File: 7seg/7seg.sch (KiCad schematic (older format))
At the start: 9 parts, among them J1 9pin_header, U1 LTS-4031JR, U2 LTS-4031JR, U3 LTS-4031JR, U4 LTS-4031JR, U5 LTS-4031JR, U6 LTS-4031JR, U7 LTS-4031JR, U8 LTS-4031JR

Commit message: 7-segment layout
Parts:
- added H1, H2, H3, H4: MountingHole, MountingHole:MountingHole_2.2mm_M2_Pad, symbol Mechanical:MountingHole
- U1, U2, U3, U4, U5, U6, U7, U8: footprint (none) -> SamacSys_Parts:DIPS762W50P254L1290H725Q10N
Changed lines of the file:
@@
 F 0 "U1" H 1550 2565 50  0000 C CNN
 F 1 "LTS-4031JR" H 1550 2474 50  0000 C CNN
-F 2 "" H 1550 2450 50  0001 C CNN
+F 2 "SamacSys_Parts:DIPS762W50P254L1290H725Q10N" H 1550 2450 50  0001 C CNN
 F 3 "" H 1550 2450 50  0001 C CNN
 	1    1550 2450
@@
 F 0 "U2" H 2750 2565 50  0000 C CNN
 F 1 "LTS-4031JR" H 2750 2474 50  0000 C CNN
-F 2 "" H 2750 2450 50  0001 C CNN
+F 2 "SamacSys_Parts:DIPS762W50P254L1290H725Q10N" H 2750 2450 50  0001 C CNN
 F 3 "" H 2750 2450 50  0001 C CNN
 	1    2750 2450
@@
 F 0 "U3" H 3950 2565 50  0000 C CNN
 F 1 "LTS-4031JR" H 3950 2474 50  0000 C CNN
-F 2 "" H 3950 2450 50  0001 C CNN
+F 2 "SamacSys_Parts:DIPS762W50P254L1290H725Q10N" H 3950 2450 50  0001 C CNN
 F 3 "" H 3950 2450 50  0001 C CNN
 	1    3950 2450
@@
 F 0 "U4" H 5150 2565 50  0000 C CNN
 F 1 "LTS-4031JR" H 5150 2474 50  0000 C CNN
-F 2 "" H 5150 2450 50  0001 C CNN
+F 2 "SamacSys_Parts:DIPS762W50P254L1290H725Q10N" H 5150 2450 50  0001 C CNN
 F 3 "" H 5150 2450 50  0001 C CNN
 	1    5150 2450
@@
 F 0 "U5" H 6300 2565 50  0000 C CNN
 F 1 "LTS-4031JR" H 6300 2474 50  0000 C CNN
-F 2 "" H 6300 2450 50  0001 C CNN
+F 2 "SamacSys_Parts:DIPS762W50P254L1290H725Q10N" H 6300 2450 50  0001 C CNN
 F 3 "" H 6300 2450 50  0001 C CNN
 	1    6300 2450
@@
 F 0 "U6" H 7450 2565 50  0000 C CNN
 F 1 "LTS-4031JR" H 7450 2474 50  0000 C CNN
-F 2 "" H 7450 2450 50  0001 C CNN
+F 2 "SamacSys_Parts:DIPS762W50P254L1290H725Q10N" H 7450 2450 50  0001 C CNN
 F 3 "" H 7450 2450 50  0001 C CNN
 	1    7450 2450
@@
 F 0 "U7" H 8600 2565 50  0000 C CNN
 F 1 "LTS-4031JR" H 8600 2474 50  0000 C CNN
-F 2 "" H 8600 2450 50  0001 C CNN
+F 2 "SamacSys_Parts:DIPS762W50P254L1290H725Q10N" H 8600 2450 50  0001 C CNN
 F 3 "" H 8600 2450 50  0001 C CNN
 	1    8600 2450
@@
 F 0 "U8" H 9750 2565 50  0000 C CNN
 F 1 "LTS-4031JR" H 9750 2474 50  0000 C CNN
-F 2 "" H 9750 2450 50  0001 C CNN
+F 2 "SamacSys_Parts:DIPS762W50P254L1290H725Q10N" H 9750 2450 50  0001 C CNN
 F 3 "" H 9750 2450 50  0001 C CNN
 	1    9750 2450
@@
 Wire Wire Line
 	6700 1700 7850 1700
+$Comp
+L Mechanical:MountingHole H1
+U 1 1 61664F25
+P 3000 750
+F 0 "H1" H 3100 796 50  0000 L CNN
+F 1 "MountingHole" H 3100 705 50  0000 L CNN
+F 2 "MountingHole:MountingHole_2.2mm_M2_Pad" H 3000 750 50  0001 C CNN
+F 3 "~" H 3000 750 50  0001 C CNN
+	1    3000 750
+	1    0    0    -1
+$EndComp
+$Comp
+L Mechanical:MountingHole H2
+U 1 1 61679F30
+P 3000 950
+F 0 "H2" H 3100 996 50  0000 L CNN
+F 1 "MountingHole" H 3100 905 50  0000 L CNN
+F 2 "MountingHole:MountingHole_2.2mm_M2_Pad" H 3000 950 50  0001 C CNN
+F 3 "~" H 3000 950 50  0001 C CNN
+	1    3000 950
+	1    0    0    -1
+$EndComp
+$Comp
+L Mechanical:MountingHole H3
+U 1 1 6167A224
+P 3000 1150
+F 0 "H3" H 3100 1196 50  0000 L CNN
+F 1 "MountingHole" H 3100 1105 50  0000 L CNN
+F 2 "MountingHole:MountingHole_2.2mm_M2_Pad" H 3000 1150 50  0001 C CNN
+F 3 "~" H 3000 1150 50  0001 C CNN
+	1    3000 1150
+	1    0    0    -1
+$EndComp
+$Comp
+L Mechanical:MountingHole H4
+U 1 1 6167A7D7
+P 3000 1350
+F 0 "H4" H 3100 1396 50  0000 L CNN
+F 1 "MountingHole" H 3100 1305 50  0000 L CNN
+F 2 "MountingHole:MountingHole_2.2mm_M2_Pad" H 3000 1350 50  0001 C CNN
+F 3 "~" H 3000 1350 50  0001 C CNN
+	1    3000 1350
+	1    0    0    -1
+$EndComp
 $EndSCHEMATC

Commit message: more library changes
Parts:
- H1, H2, H3, H4: footprint MountingHole:MountingHole_2.2mm_M2_Pad -> footprints:MountingHole_2.2mm_M2_Pad
- J1: footprint HDRV9W63P0X254_1X9_2286X369X950P -> footprints:header
- U1, U2, U3, U4, U5, U6, U7, U8: footprint SamacSys_Parts:DIPS762W50P254L1290H725Q10N -> footprints:7seg
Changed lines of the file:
@@
 F 0 "U1" H 1550 2565 50  0000 C CNN
 F 1 "LTS-4031JR" H 1550 2474 50  0000 C CNN
-F 2 "SamacSys_Parts:DIPS762W50P254L1290H725Q10N" H 1550 2450 50  0001 C CNN
+F 2 "footprints:7seg" H 1550 2450 50  0001 C CNN
 F 3 "" H 1550 2450 50  0001 C CNN
 	1    1550 2450
-	1    0    0    -1
-$EndComp
-$Comp
-L 477_7seg_symbols:LTS-4031JR U2
-U 1 1 615ED9B1
-P 2750 2450
-F 0 "U2" H 2750 2565 50  0000 C CNN
-F 1 "LTS-4031JR" H 2750 2474 50  0000 C CNN
-F 2 "SamacSys_Parts:DIPS762W50P254L1290H725Q10N" H 2750 2450 50  0001 C CNN
-F 3 "" H 2750 2450 50  0001 C CNN
-	1    2750 2450
-	1    0    0    -1
-$EndComp
-$Comp
-L 477_7seg_symbols:LTS-4031JR U3
-U 1 1 615EE8CF
-P 3950 2450
-F 0 "U3" H 3950 2565 50  0000 C CNN
-F 1 "LTS-4031JR" H 3950 2474 50  0000 C CNN
-F 2 "SamacSys_Parts:DIPS762W50P254L1290H725Q10N" H 3950 2450 50  0001 C CNN
-F 3 "" H 3950 2450 50  0001 C CNN
-	1    3950 2450
-	1    0    0    -1
-$EndComp
-$Comp
-L 477_7seg_symbols:LTS-4031JR U4
-U 1 1 615EF228
-P 5150 2450
-F 0 "U4" H 5150 2565 50  0000 C CNN
-F 1 "LTS-4031JR" H 5150 2474 50  0000 C CNN
-F 2 "SamacSys_Parts:DIPS762W50P254L1290H725Q10N" H 5150 2450 50  0001 C CNN
-F 3 "" H 5150 2450 50  0001 C CNN
-	1    5150 2450
-	1    0    0    -1
-$EndComp
-$Comp
-L 477_7seg_symbols:LTS-4031JR U5
-U 1 1 615F0325
-P 6300 2450
-F 0 "U5" H 6300 2565 50  0000 C CNN
-F 1 "LTS-4031JR" H 6300 2474 50  0000 C CNN
-F 2 "SamacSys_Parts:DIPS762W50P254L1290H725Q10N" H 6300 2450 50  0001 C CNN
-F 3 "" H 6300 2450 50  0001 C CNN
-	1    6300 2450
-	1    0    0    -1
-$EndComp
-$Comp
-L 477_7seg_symbols:LTS-4031JR U6
-U 1 1 615F0C91
-P 7450 2450
-F 0 "U6" H 7450 2565 50  0000 C CNN
-F 1 "LTS-4031JR" H 7450 2474 50  0000 C CNN
-F 2 "SamacSys_Parts:DIPS762W50P254L1290H725Q10N" H 7450 2450 50  0001 C CNN
-F 3 "" H 7450 2450 50  0001 C CNN
-	1    7450 2450
-	1    0    0    -1
-$EndComp
-$Comp
-L 477_7seg_symbols:LTS-4031JR U7
-U 1 1 615F27E9
-P 8600 2450
-F 0 "U7" H 8600 2565 50  0000 C CNN
-F 1 "LTS-4031JR" H 8600 2474 50  0000 C CNN
-F 2 "SamacSys_Parts:DIPS762W50P254L1290H725Q10N" H 8600 2450 50  0001 C CNN
-F 3 "" H 8600 2450 50  0001 C CNN
-	1    8600 2450
-	1    0    0    -1
-$EndComp
-$Comp
-L 477_7seg_symbols:LTS-4031JR U8
-U 1 1 615F702E
-P 9750 2450
-F 0 "U8" H 9750 2565 50  0000 C CNN
-F 1 "LTS-4031JR" H 9750 2474 50  0000 C CNN
-F 2 "SamacSys_Parts:DIPS762W50P254L1290H725Q10N" H 9750 2450 50  0001 C CNN
-F 3 "" H 9750 2450 50  0001 C CNN
-	1    9750 2450
 	1    0    0    -1
 $EndComp
@@
 F 0 "J1" V 5488 672 50  0000 R CNN
 F 1 "9pin_header" V 5397 672 50  0000 R CNN
-F 2 "HDRV9W63P0X254_1X9_2286X369X950P" H 5800 1700 50  0001 L CNN
+F 2 "footprints:header" H 5800 1700 50  0001 L CNN
 F 3 "https://componentsearchengine.com/Datasheets/1/825433-9.pdf" H 5800 1600 50  0001 L CNN
 F 4 "MOD 2 PINHDR 1X9 P." H 5800 1500 50  0001 L CNN "Description"
@@
 	6700 1700 7850 1700
 $Comp
-L Mechanical:MountingHole H1
-U 1 1 61664F25
-P 3000 750
-F 0 "H1" H 3100 796 50  0000 L CNN
-F 1 "MountingHole" H 3100 705 50  0000 L CNN
-F 2 "MountingHole:MountingHole_2.2mm_M2_Pad" H 3000 750 50  0001 C CNN
-F 3 "~" H 3000 750 50  0001 C CNN
-	1    3000 750
-	1    0    0    -1
-$EndComp
-$Comp
-L Mechanical:MountingHole H2
-U 1 1 61679F30
-P 3000 950
-F 0 "H2" H 3100 996 50  0000 L CNN
-F 1 "MountingHole" H 3100 905 50  0000 L CNN
-F 2 "MountingHole:MountingHole_2.2mm_M2_Pad" H 3000 950 50  0001 C CNN
-F 3 "~" H 3000 950 50  0001 C CNN
-	1    3000 950
-	1    0    0    -1
-$EndComp
-$Comp
-L Mechanical:MountingHole H3
-U 1 1 6167A224
-P 3000 1150
-F 0 "H3" H 3100 1196 50  0000 L CNN
-F 1 "MountingHole" H 3100 1105 50  0000 L CNN
-F 2 "MountingHole:MountingHole_2.2mm_M2_Pad" H 3000 1150 50  0001 C CNN
-F 3 "~" H 3000 1150 50  0001 C CNN
-	1    3000 1150
-	1    0    0    -1
-$EndComp
-$Comp
 L Mechanical:MountingHole H4
 U 1 1 6167A7D7
@@
 F 0 "H4" H 3100 1396 50  0000 L CNN
 F 1 "MountingHole" H 3100 1305 50  0000 L CNN
-F 2 "MountingHole:MountingHole_2.2mm_M2_Pad" H 3000 1350 50  0001 C CNN
+F 2 "footprints:MountingHole_2.2mm_M2_Pad" H 3000 1350 50  0001 C CNN
 F 3 "~" H 3000 1350 50  0001 C CNN
 	1    3000 1350
 	1    0    0    -1
 $EndComp
+$Comp
+L 477_7seg_symbols:LTS-4031JR U2
+U 1 1 61670141
+P 2750 2450
+F 0 "U2" H 2750 2565 50  0000 C CNN
+F 1 "LTS-4031JR" H 2750 2474 50  0000 C CNN
+F 2 "footprints:7seg" H 2750 2450 50  0001 C CNN
+F 3 "" H 2750 2450 50  0001 C CNN
+	1    2750 2450
+	1    0    0    -1
+$EndComp
+$Comp
+L 477_7seg_symbols:LTS-4031JR U3
+U 1 1 61670C1A
+P 3950 2450
+F 0 "U3" H 3950 2565 50  0000 C CNN
+F 1 "LTS-4031JR" H 3950 2474 50  0000 C CNN
+F 2 "footprints:7seg" H 3950 2450 50  0001 C CNN
+F 3 "" H 3950 2450 50  0001 C CNN
+	1    3950 2450
+	1    0    0    -1
+$EndComp
+$Comp
+L 477_7seg_symbols:LTS-4031JR U4
+U 1 1 616713BD
+P 5150 2450
+F 0 "U4" H 5150 2565 50  0000 C CNN
+F 1 "LTS-4031JR" H 5150 2474 50  0000 C CNN
+F 2 "footprints:7seg" H 5150 2450 50  0001 C CNN
+F 3 "" H 5150 2450 50  0001 C CNN
+	1    5150 2450
+	1    0    0    -1
+$EndComp
+$Comp
+L 477_7seg_symbols:LTS-4031JR U5
+U 1 1 616717C6
+P 6300 2450
+F 0 "U5" H 6300 2565 50  0000 C CNN
+F 1 "LTS-4031JR" H 6300 2474 50  0000 C CNN
+F 2 "footprints:7seg" H 6300 2450 50  0001 C CNN
+F 3 "" H 6300 2450 50  0001 C CNN
+	1    6300 2450
+	1    0    0    -1
+$EndComp
+$Comp
+L 477_7seg_symbols:LTS-4031JR U6
+U 1 1 61671D60
+P 7450 2450
+F 0 "U6" H 7450 2565 50  0000 C CNN
+F 1 "LTS-4031JR" H 7450 2474 50  0000 C CNN
+F 2 "footprints:7seg" H 7450 2450 50  0001 C CNN
+F 3 "" H 7450 2450 50  0001 C CNN
+	1    7450 2450
+	1    0    0    -1
+$EndComp
+$Comp
+L 477_7seg_symbols:LTS-4031JR U7
+U 1 1 616722D6
+P 8600 2450
+F 0 "U7" H 8600 2565 50  0000 C CNN
+F 1 "LTS-4031JR" H 8600 2474 50  0000 C CNN
+F 2 "footprints:7seg" H 8600 2450 50  0001 C CNN
+F 3 "" H 8600 2450 50  0001 C CNN
+	1    8600 2450
+	1    0    0    -1
+$EndComp
+$Comp
+L 477_7seg_symbols:LTS-4031JR U8
+U 1 1 6167297B
+P 9750 2450
+F 0 "U8" H 9750 2565 50  0000 C CNN
+F 1 "LTS-4031JR" H 9750 2474 50  0000 C CNN
+F 2 "footprints:7seg" H 9750 2450 50  0001 C CNN
+F 3 "" H 9750 2450 50  0001 C CNN
+	1    9750 2450
+	1    0    0    -1
+$EndComp
+$Comp
+L Mechanical:MountingHole H3
+U 1 1 616872D0
+P 3000 1150
+F 0 "H3" H 3100 1196 50  0000 L CNN
+F 1 "MountingHole" H 3100 1105 50  0000 L CNN
+F 2 "footprints:MountingHole_2.2mm_M2_Pad" H 3000 1150 50  0001 C CNN
+F 3 "~" H 3000 1150 50  0001 C CNN
+	1    3000 1150
+	1    0    0    -1
+$EndComp
+$Comp
+L Mechanical:MountingHole H2
+U 1 1 616873EF
+P 3000 950
+F 0 "H2" H 3100 996 50  0000 L CNN
+F 1 "MountingHole" H 3100 905 50  0000 L CNN
+F 2 "footprints:MountingHole_2.2mm_M2_Pad" H 3000 950 50  0001 C CNN
+F 3 "~" H 3000 950 50  0001 C CNN
+	1    3000 950
+	1    0    0    -1
+$EndComp
+$Comp
+L Mechanical:MountingHole H1
+U 1 1 61687670
+P 3000 750
+F 0 "H1" H 3100 796 50  0000 L CNN
+F 1 "MountingHole" H 3100 705 50  0000 L CNN
+F 2 "footprints:MountingHole_2.2mm_M2_Pad" H 3000 750 50  0001 C CNN
+F 3 "~" H 3000 750 50  0001 C CNN
+	1    3000 750
+	1    0    0    -1
+$EndComp

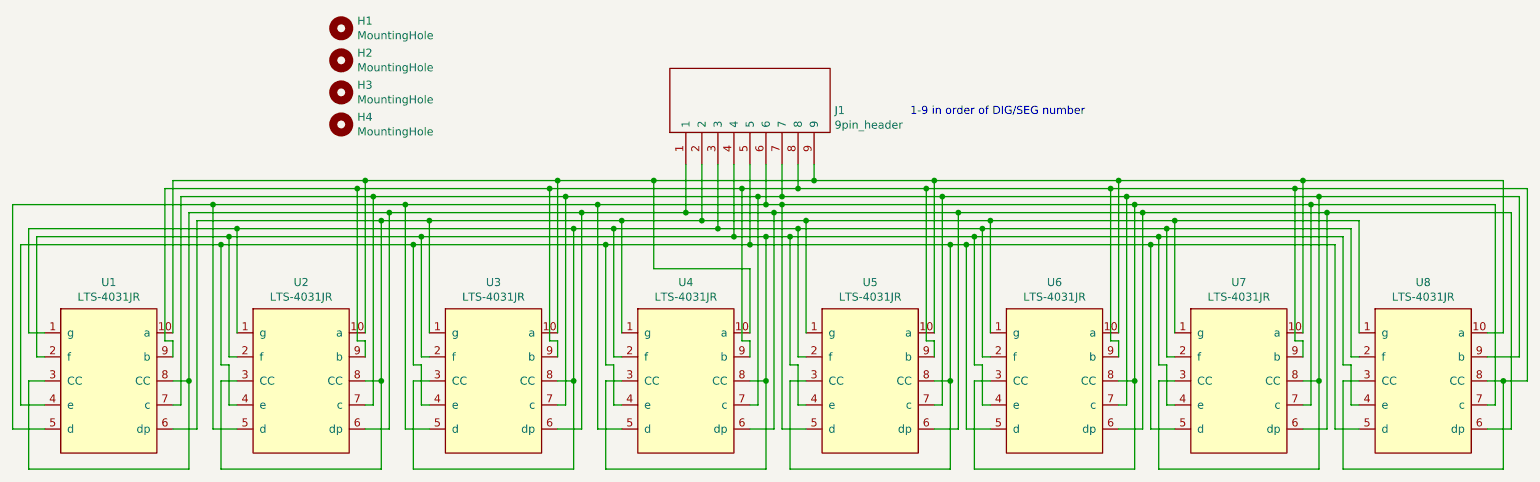
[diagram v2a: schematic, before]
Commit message: Added reset button, fixed 7seg pin order
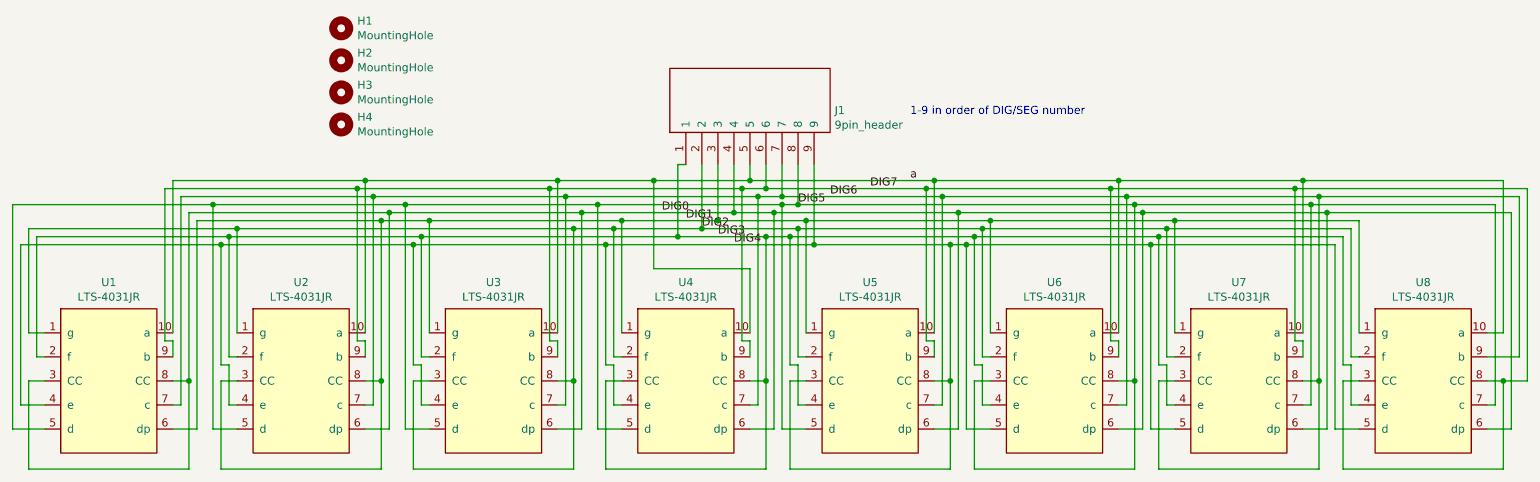
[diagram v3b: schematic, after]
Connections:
- net DIG2: now reaches U1.1 (g), U2.1 (g), U3.3 (CC), U3.8 (CC), U4.2 (f), U5.2 (f), U6.2 (f), U7.2 (f), U8.2 (f)
- net DIG2: now also J1.2; no longer J1.3
- net a: now reaches U1.10 (a), U2.10 (a), U3.10 (a), U4.10 (a), U5.10 (a), U6.10 (a), U7.10 (a), U8.10 (a)
- net a: now also J1.5; no longer J1.9
- net DIG3: now reaches U1.2 (f), U2.2 (f), U3.2 (f), U4.3 (CC), U4.8 (CC), U5.4 (e), U6.4 (e), U7.4 (e), U8.4 (e)
- net DIG3: now also J1.1; no longer J1.4
- net DIG0: now reaches U1.3 (CC), U1.8 (CC), U2.6 (dp), U3.6 (dp), U4.6 (dp), U5.6 (dp), U6.6 (dp), U7.6 (dp), U8.6 (dp)
- net DIG0: now also J1.4; no longer J1.1
- net DIG4: now reaches U1.4 (e), U2.4 (e), U3.4 (e), U4.4 (e), U5.3 (CC), U5.8 (CC), U6.5 (d), U7.5 (d), U8.5 (d)
- net DIG4: now also J1.9; no longer J1.5
- net DIG5: now reaches U1.5 (d), U2.5 (d), U3.5 (d), U4.5 (d), U5.5 (d), U6.3 (CC), U6.8 (CC), U7.7 (c), U8.7 (c)
- net DIG5: now also J1.8; no longer J1.6
- net DIG1: now reaches U1.6 (dp), U2.3 (CC), U2.8 (CC), U3.1 (g), U4.1 (g), U5.1 (g), U6.1 (g), U7.1 (g), U8.1 (g)
- net DIG1: now also J1.3; no longer J1.2
- net DIG6: now reaches J1.7, U1.7 (c), U2.7 (c), U3.7 (c), U4.7 (c), U5.7 (c), U6.7 (c), U7.3 (CC), U7.8 (CC), U8.9 (b)
- net DIG7: now reaches U1.9 (b), U2.9 (b), U3.9 (b), U4.9 (b), U5.9 (b), U6.9 (b), U7.9 (b), U8.3 (CC), U8.8 (CC)
- net DIG7: now also J1.6; no longer J1.8
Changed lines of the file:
@@
 	10250 2950 10150 2950
-Wire Wire Line
-	5150 1900 4500 1900
 Wire Wire Line
 	3150 3250 3300 3250
@@
 	4500 1900 3300 1900
 Wire Wire Line
-	5150 1900 5700 1900
-Wire Wire Line
 	10300 1900 10300 3250
 Wire Wire Line
 	10300 3250 10150 3250
-Connection ~ 5150 1900
 Wire Wire Line
 	9000 3250 9150 3250
@@
 Wire Wire Line
 	5700 1900 6850 1900
-Wire Wire Line
-	5250 1950 4750 1950
 Wire Wire Line
 	2100 1950 2100 3250
@@
 	4750 1950 3550 1950
 Wire Wire Line
-	5250 1950 5900 1950
-Wire Wire Line
 	9350 1950 9350 2650
-Connection ~ 5250 1950
 Wire Wire Line
 	8200 2650 8200 1950
@@
 Wire Wire Line
 	5900 1950 7050 1950
-Wire Wire Line
-	5350 2000 4700 2000
 Wire Wire Line
 	1050 2000 1050 2650
@@
 	4700 2000 4450 2000
 Wire Wire Line
-	5350 2000 5850 2000
-Wire Wire Line
 	9300 2000 9300 2800
 Wire Wire Line
 	9300 2800 9350 2800
-Connection ~ 5350 2000
 Wire Wire Line
 	5900 2800 5850 2800
@@
 	8150 2000 9300 2000
 Wire Wire Line
-	5450 2050 3500 2050
-Wire Wire Line
 	1100 2050 1100 2800
 Wire Wire Line
@@
 Wire Wire Line
 	5650 2950 5650 2050
-Wire Wire Line
-	5650 2050 5450 2050
 Connection ~ 5650 2950
-Connection ~ 5450 2050
 Wire Wire Line
 	5650 2050 5800 2050
@@
 	5800 2050 6950 2050
 Wire Wire Line
-	5550 2100 4650 2100
-Wire Wire Line
 	1000 2100 1000 3100
 Wire Wire Line
@@
 Wire Wire Line
 	6800 2950 6800 2100
-Wire Wire Line
-	6800 2100 5550 2100
 Connection ~ 6800 2950
-Connection ~ 5550 2100
 Wire Wire Line
 	6800 2100 6900 2100
@@
 	4500 3250 4500 1900
 Wire Wire Line
-	5150 1600 5150 1900
-Wire Wire Line
-	5250 1600 5250 1950
-Wire Wire Line
-	5350 1600 5350 2000
-Wire Wire Line
-	5450 1600 5450 2050
-Wire Wire Line
-	5550 1600 5550 2100
-Wire Wire Line
-	5650 1600 5650 1850
-Wire Wire Line
-	5650 1850 4600 1850
-Wire Wire Line
 	950  1850 950  3250
 Wire Wire Line
@@
 Wire Wire Line
 	5750 3250 5750 1850
-Wire Wire Line
-	5750 1850 5650 1850
-Connection ~ 5650 1850
 Wire Wire Line
 	7950 2950 7950 1850
@@
 Connection ~ 9050 1850
 Wire Wire Line
-	5750 1600 5750 1800
-Wire Wire Line
-	5750 1800 5600 1800
-Wire Wire Line
 	2000 1800 2000 3100
 Wire Wire Line
@@
 	5600 1800 4400 1800
 Wire Wire Line
-	7950 1850 5750 1850
-Wire Wire Line
-	5750 1800 6750 1800
+	7950 1850 5850 1850
 Wire Wire Line
 	10350 1800 10350 2800
 Wire Wire Line
 	10350 2800 10150 2800
-Connection ~ 5750 1800
 Wire Wire Line
 	9100 2950 9100 1800
@@
 	6750 1800 7900 1800
 Wire Wire Line
-	5850 1600 5850 1750
-Wire Wire Line
-	5850 1750 6650 1750
-Wire Wire Line
 	10400 1750 10400 2950
 Wire Wire Line
@@
 Connection ~ 6650 1750
 Wire Wire Line
-	5850 1750 5500 1750
-Wire Wire Line
 	1900 1750 1900 2700
 Wire Wire Line
@@
 Wire Wire Line
 	1950 2700 1950 2800
-Connection ~ 5850 1750
 Wire Wire Line
 	3150 2800 3150 2700
@@
 	5500 1750 4300 1750
 Wire Wire Line
-	5950 1600 5950 1700
-Wire Wire Line
-	5950 1700 4950 1700
-Wire Wire Line
 	1950 1700 1950 2650
 Wire Wire Line
@@
 	6650 1750 7800 1750
 Wire Wire Line
-	5950 1700 6700 1700
-Wire Wire Line
 	10250 1700 10250 2650
 Wire Wire Line
 	10250 2650 10150 2650
-Connection ~ 5950 1700
 Wire Wire Line
 	9000 2650 9000 1700
@@
 	1    0    0    -1
 $EndComp
+Text Label 5000 1900 0    50   ~ 0
+DIG0
+Text Label 5250 2000 0    50   ~ 0
+DIG2
+Text Label 5350 2050 0    50   ~ 0
+DIG3
+Text Label 5450 2100 0    50   ~ 0
+DIG4
+Text Label 5850 1850 0    50   ~ 0
+DIG5
+Text Label 6050 1800 0    50   ~ 0
+DIG6
+Text Label 6300 1750 0    50   ~ 0
+DIG7
+Text Label 5150 1950 0    50   ~ 0
+DIG1
+Text Label 6550 1700 0    50   ~ 0
+a
+Wire Wire Line
+	4500 1900 5450 1900
+Wire Wire Line
+	4700 2000 5250 2000
+Wire Wire Line
+	4650 2100 5950 2100
+Wire Wire Line
+	4600 1850 5750 1850
+Wire Wire Line
+	5600 1800 5750 1800
+Wire Wire Line
+	4950 1700 5550 1700
+Wire Wire Line
+	5450 1600 5450 1900
+Connection ~ 5450 1900
+Wire Wire Line
+	5450 1900 5700 1900
+Wire Wire Line
+	5350 1600 5350 1950
+Connection ~ 5350 1950
+Wire Wire Line
+	5350 1950 5900 1950
+Wire Wire Line
+	5250 1600 5250 2000
+Connection ~ 5250 2000
+Wire Wire Line
+	5250 2000 5850 2000
+Wire Wire Line
+	4750 1950 5350 1950
+Wire Wire Line
+	3500 2050 5100 2050
+Wire Wire Line
+	5150 1600 5100 1600
+Wire Wire Line
+	5100 1600 5100 2050
+Connection ~ 5100 2050
+Wire Wire Line
+	5100 2050 5650 2050
+Wire Wire Line
+	5950 1600 5950 2100
+Connection ~ 5950 2100
+Wire Wire Line
+	5950 2100 6800 2100
+Wire Wire Line
+	5850 1600 5850 1850
+Connection ~ 5850 1850
+Wire Wire Line
+	5850 1850 5750 1850
+Wire Wire Line
+	5500 1750 5650 1750
+Wire Wire Line
+	5750 1600 5750 1800
+Connection ~ 5750 1800
+Wire Wire Line
+	5750 1800 6750 1800
+Wire Wire Line
+	5650 1600 5650 1750
+Connection ~ 5650 1750
+Wire Wire Line
+	5650 1750 6650 1750
+Wire Wire Line
+	5550 1600 5550 1700
+Connection ~ 5550 1700
+Wire Wire Line
+	5550 1700 6700 1700
 $EndSCHEMATC
